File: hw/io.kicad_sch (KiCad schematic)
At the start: 30 parts, among them J2 CFMASTER, J3 AVR-ISP, J4 ACTLED, U12 ATmega328PB-A, U13 cfconn, U14 ATA0, U15 mouse, U16 kbd, U17 ds1501, U18 mc68681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

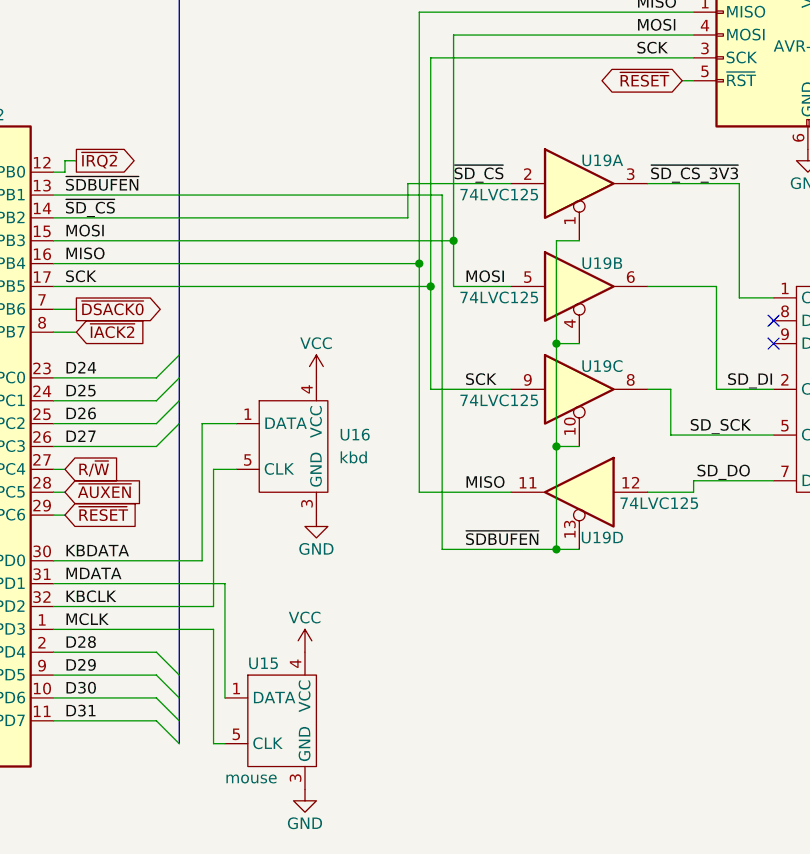
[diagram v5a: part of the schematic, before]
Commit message: added shield pin in ps2conn symbol, fixed ERC
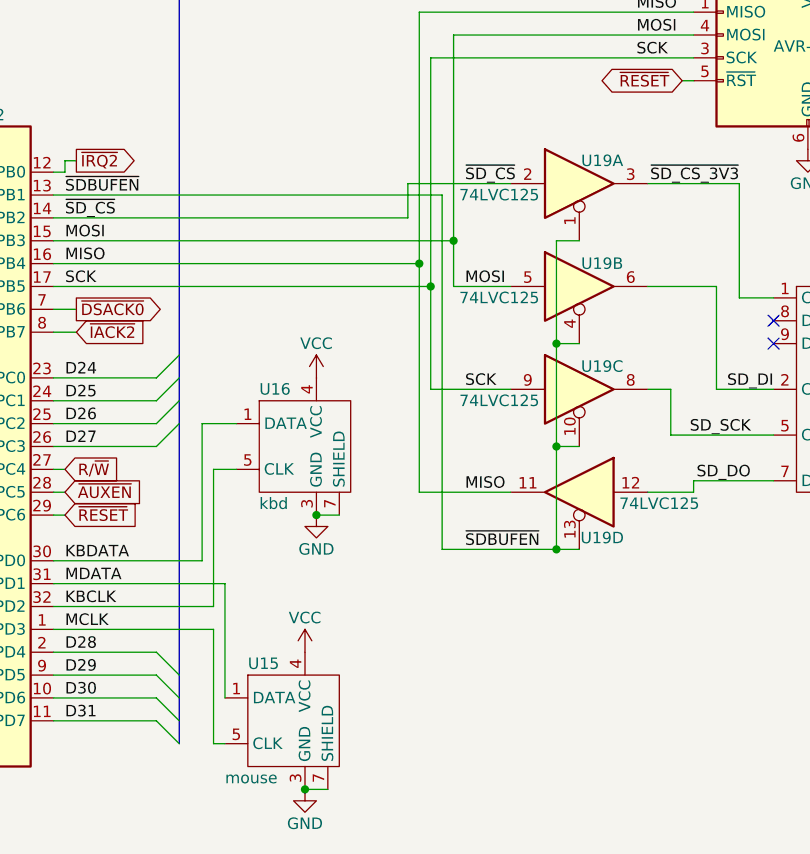
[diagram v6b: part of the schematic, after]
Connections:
- net GND: now also U15.7 (SHIELD), U16.7 (SHIELD)
- net MOSI: no longer U12.14 (PB2), U19.2
- new net ~{SD_CS}: U12.14 (PB2), U19.2
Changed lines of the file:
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@@
   (junction (at 92.71 170.18) (diameter 0) (color 0 0 0 0)
   )
+  (junction (at 85.09 276.86) (diameter 0) (color 0 0 0 0)
+  )
   (junction (at 30.48 176.53) (diameter 0) (color 0 0 0 0)
   )
@@
   (junction (at 99.06 95.25) (diameter 0) (color 0 0 0 0)
   )
+  (junction (at 86.36 246.38) (diameter 0) (color 0 0 0 0)
+  )
   (junction (at 142.24 129.54) (diameter 0) (color 0 0 0 0)
   )
@@
     (stroke (width 0) (type default) (color 0 0 0 0))
   )
+  (wire (pts (xy 96.52 209.55) (xy 107.95 209.55))
+    (stroke (width 0) (type default) (color 0 0 0 0))
+  )
   (wire (pts (xy 57.15 213.36) (xy 96.52 213.36))
     (stroke (width 0) (type default) (color 0 0 0 0))
@@
     (stroke (width 0) (type default) (color 0 0 0 0))
   )
-  (wire (pts (xy 96.52 209.55) (xy 107.95 209.55))
-    (stroke (width 0) (type default) (color 0 0 0 0))
-  )
   (wire (pts (xy 128.27 242.57) (xy 137.16 242.57))
     (stroke (width 0) (type default) (color 0 0 0 0))
@@
     (stroke (width 0) (type default) (color 0 0 0 0))
   )
+  (wire (pts (xy 85.09 276.86) (xy 87.63 276.86))
+    (stroke (width 0) (type default) (color 0 0 0 0))
+  )
   (wire (pts (xy 26.67 39.37) (xy 33.02 39.37))
     (stroke (width 0) (type default) (color 0 0 0 0))
@@
     (stroke (width 0) (type default) (color 0 0 0 0))
   )
+  (wire (pts (xy 86.36 246.38) (xy 88.9 246.38))
+    (stroke (width 0) (type default) (color 0 0 0 0))
+  )
   (wire (pts (xy 132.08 76.2) (xy 132.08 46.99))
     (stroke (width 0) (type default) (color 0 0 0 0))
@@
     (effects (font (size 1.27 1.27)) (justify left bottom))
   )
-  (label "~{SD_CS}" (at 101.6 209.55 0)
+  (label "~{SD_CS}" (at 102.87 209.55 0)
     (effects (font (size 1.27 1.27)) (justify left bottom))
   )
@@
     (pin "5")
     (pin "6")
+    (pin "7")
   )
   (symbol (lib_id "Device:Crystal_Small") (at 92.71 162.56 90) (unit 1)
@@
   )
   (symbol (lib_id "m68kcomp2:ps2conn") (at 85.09 238.76 0) (unit 1)
-    (in_bom yes) (on_board yes) (fields_autoplaced)
-    (property "Reference" "U16" (id 0) (at 88.9 237.4899 0)
+    (in_bom yes) (on_board yes)
+    (property "Reference" "U16" (id 0) (at 80.01 232.41 0)
       (effects (font (size 1.27 1.27)) (justify left))
     )
-    (property "Value" "kbd" (id 1) (at 88.9 240.0299 0)
+    (property "Value" "kbd" (id 1) (at 80.01 245.11 0)
       (effects (font (size 1.27 1.27)) (justify left))
     )
@@
     (pin "5")
     (pin "6")
+    (pin "7")
   )
   (symbol (lib_id "power:GND") (at 143.51 99.06 0) (unit 1)

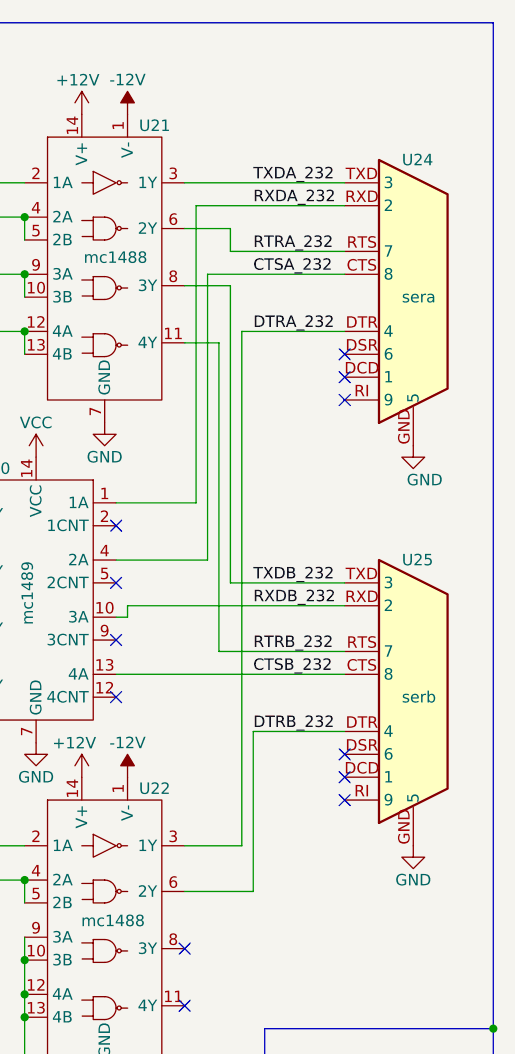
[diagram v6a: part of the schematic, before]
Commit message: fixed swapped pin-name/number fields in rs232 connector symbol
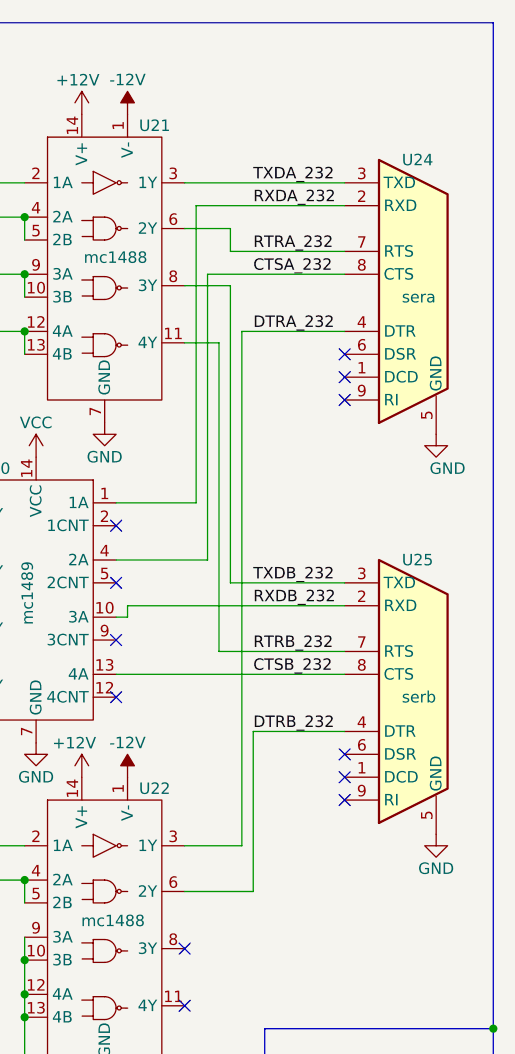
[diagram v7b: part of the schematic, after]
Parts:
- U24, U25: footprint Connector_Dsub:DSUB-9_Male_Horizontal_P2.77x2.54mm_EdgePinOffset9.40mm -> Connector_Dsub:DSUB-9_Male_Horizontal_P2.77x2.84mm_EdgePinOffset7.70mm_Housed_MountingHolesOffset9.12mm
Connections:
- net CTSA_232: now also U24.8 (CTS); no longer U24.CTS (8)
- net CTSB_232: now also U25.8 (CTS); no longer U25.CTS (8)
- net DTRA_232: now also U24.4 (DTR); no longer U24.DTR (4)
- net DTRB_232: now also U25.4 (DTR); no longer U25.DTR (4)
- net GND: now also U24.5 (GND), U25.5 (GND); no longer U24.GND (5), U25.GND (5)
- net RTRA_232: now also U24.7 (RTS); no longer U24.RTS (7)
- net RTRB_232: now also U25.7 (RTS); no longer U25.RTS (7)
- net RXDA_232: now also U24.2 (RXD); no longer U24.RXD (2)
- net RXDB_232: now also U25.2 (RXD); no longer U25.RXD (2)
- net TXDA_232: now also U24.3 (TXD); no longer U24.TXD (3)
- net TXDB_232: now also U25.3 (TXD); no longer U25.TXD (3)
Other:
- moved on the sheet: U24, U25
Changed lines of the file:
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@@
     (pin "1")
   )
-  (symbol (lib_id "power:GND") (at 185.42 110.49 0) (unit 1)
-    (in_bom yes) (on_board yes)
-    (property "Reference" "#PWR065" (id 0) (at 185.42 116.84 0)
-      (effects (font (size 1.27 1.27)) hide)
-    )
-    (property "Value" "GND" (id 1) (at 185.42 114.3 0))
-    (property "Footprint" "" (id 2) (at 185.42 110.49 0)
-      (effects (font (size 1.27 1.27)) hide)
-    )
-    (property "Datasheet" "" (id 3) (at 185.42 110.49 0)
+  (symbol (lib_id "power:GND") (at 187.96 109.22 0) (unit 1)
+    (in_bom yes) (on_board yes)
+    (property "Reference" "#PWR065" (id 0) (at 187.96 115.57 0)
+      (effects (font (size 1.27 1.27)) hide)
+    )
+    (property "Value" "GND" (id 1) (at 187.96 113.03 0))
+    (property "Footprint" "" (id 2) (at 187.96 109.22 0)
+      (effects (font (size 1.27 1.27)) hide)
+    )
+    (property "Datasheet" "" (id 3) (at 187.96 109.22 0)
       (effects (font (size 1.27 1.27)) hide)
     )
@@
     (pin "1")
   )
-  (symbol (lib_id "power:GND") (at 185.42 66.04 0) (unit 1)
-    (in_bom yes) (on_board yes)
-    (property "Reference" "#PWR064" (id 0) (at 185.42 72.39 0)
-      (effects (font (size 1.27 1.27)) hide)
-    )
-    (property "Value" "GND" (id 1) (at 186.69 69.85 0))
-    (property "Footprint" "" (id 2) (at 185.42 66.04 0)
-      (effects (font (size 1.27 1.27)) hide)
-    )
-    (property "Datasheet" "" (id 3) (at 185.42 66.04 0)
+  (symbol (lib_id "power:GND") (at 187.96 64.77 0) (unit 1)
+    (in_bom yes) (on_board yes)
+    (property "Reference" "#PWR064" (id 0) (at 187.96 71.12 0)
+      (effects (font (size 1.27 1.27)) hide)
+    )
+    (property "Value" "GND" (id 1) (at 189.23 68.58 0))
+    (property "Footprint" "" (id 2) (at 187.96 64.77 0)
+      (effects (font (size 1.27 1.27)) hide)
+    )
+    (property "Datasheet" "" (id 3) (at 187.96 64.77 0)
       (effects (font (size 1.27 1.27)) hide)
     )
@@
     (pin "1")
   )
-  (symbol (lib_id "m68kcomp2:rs232_conn") (at 185.42 34.29 0) (unit 1)
+  (symbol (lib_name "rs232_conn_1") (lib_id "m68kcomp2:rs232_conn") (at 185.42 34.29 0) (unit 1)
     (in_bom yes) (on_board yes)
     (property "Reference" "U24" (id 0) (at 184.15 34.29 0)
@@
       (effects (font (size 1.27 1.27)) (justify left))
     )
-    (property "Footprint" "Connector_Dsub:DSUB-9_Male_Horizontal_P2.77x2.54mm_EdgePinOffset9.40mm" (id 2) (at 185.42 34.29 0)
+    (property "Footprint" "Connector_Dsub:DSUB-9_Male_Horizontal_P2.77x2.84mm_EdgePinOffset7.70mm_Housed_MountingHolesOffset9.12mm" (id 2) (at 185.42 34.29 0)
       (effects (font (size 1.27 1.27)) hide)
     )
@@
       (effects (font (size 1.27 1.27)) hide)
     )
-    (pin "CTS")
-    (pin "DCD")
-    (pin "DSR")
-    (pin "DTR")
-    (pin "GND")
-    (pin "RI")
-    (pin "RTS")
-    (pin "RXD")
-    (pin "TXD")
+    (pin "1")
+    (pin "2")
+    (pin "3")
+    (pin "4")
+    (pin "5")
+    (pin "6")
+    (pin "7")
+    (pin "8")
+    (pin "9")
   )
   (symbol (lib_id "power:VCC") (at 162.56 160.02 0) (unit 1)
@@
       (effects (font (size 1.27 1.27)) (justify left))
     )
-    (property "Footprint" "Connector_Dsub:DSUB-9_Male_Horizontal_P2.77x2.54mm_EdgePinOffset9.40mm" (id 2) (at 185.42 78.74 0)
+    (property "Footprint" "Connector_Dsub:DSUB-9_Male_Horizontal_P2.77x2.84mm_EdgePinOffset7.70mm_Housed_MountingHolesOffset9.12mm" (id 2) (at 185.42 78.74 0)
       (effects (font (size 1.27 1.27)) hide)
     )
@@
       (effects (font (size 1.27 1.27)) hide)
     )
-    (pin "CTS")
-    (pin "DCD")
-    (pin "DSR")
-    (pin "DTR")
-    (pin "GND")
-    (pin "RI")
-    (pin "RTS")
-    (pin "RXD")
-    (pin "TXD")
+    (pin "1")
+    (pin "2")
+    (pin "3")
+    (pin "4")
+    (pin "5")
+    (pin "6")
+    (pin "7")
+    (pin "8")
+    (pin "9")
   )
   (symbol (lib_id "power:GND") (at 109.22 109.22 0) (unit 1)

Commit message: fixed resistor footprint assignments, changed PCB to 4-layer
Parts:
- R5, R6, R7: footprint OptoDevice:R_LDR_D13.8mm_P9.0mm_Vertical -> Resistor_SMD:R_0805_2012Metric_Pad1.20x1.40mm_HandSolder
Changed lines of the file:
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@@
       (effects (font (size 1.27 1.27)) (justify left))
     )
-    (property "Footprint" "OptoDevice:R_LDR_D13.8mm_P9.0mm_Vertical" (id 2) (at 74.422 144.78 90)
+    (property "Footprint" "Resistor_SMD:R_0805_2012Metric_Pad1.20x1.40mm_HandSolder" (id 2) (at 74.422 144.78 90)
       (effects (font (size 1.27 1.27)) hide)
     )
@@
       (effects (font (size 1.27 1.27)) (justify left))
     )
-    (property "Footprint" "OptoDevice:R_LDR_D13.8mm_P9.0mm_Vertical" (id 2) (at 149.86 159.512 90)
+    (property "Footprint" "Resistor_SMD:R_0805_2012Metric_Pad1.20x1.40mm_HandSolder" (id 2) (at 149.86 159.512 90)
       (effects (font (size 1.27 1.27)) hide)
     )
@@
       (effects (font (size 1.27 1.27)) (justify left))
     )
-    (property "Footprint" "OptoDevice:R_LDR_D13.8mm_P9.0mm_Vertical" (id 2) (at 149.86 165.862 90)
-      (effects (font (size 1.27 1.27)) hide)
-    )
+    (property "Footprint" "Resistor_SMD:R_0805_2012Metric_Pad1.20x1.40mm_HandSolder" (id 2) (at 149.86 165.862 90)
+      (effects (font (size 1.27 1.27)) hide)
+    )
